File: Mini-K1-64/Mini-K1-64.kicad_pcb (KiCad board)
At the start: 2 copper layers, 55 x 44.6 mm, 47 parts, among them J2 Conn_01x16_Pin, J3 Conn_01x16_Pin, J4 Conn_01x16_Pin, J5 Conn_01x16_Pin, P1 USB_C_Plug_USB2.0, SW1 KEY, U1 CH343G, U2 FS32K144HAT0MLHT, U3 AMS1117-3.3, Y1 8M

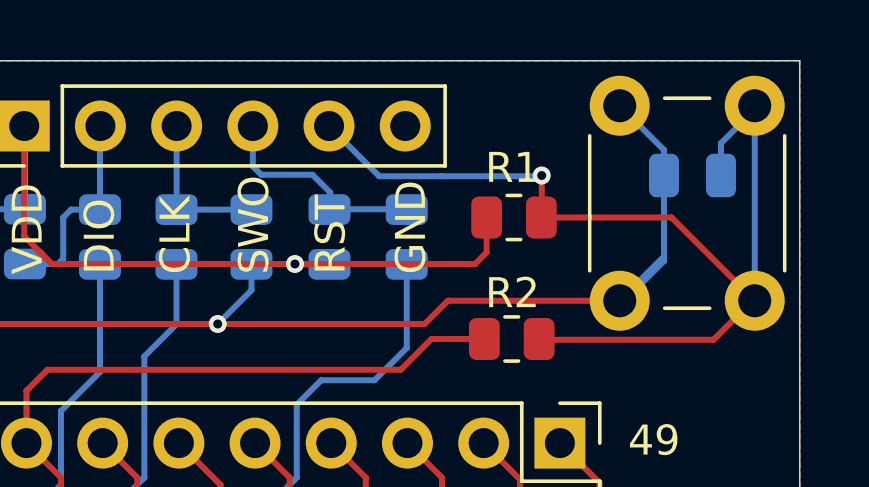
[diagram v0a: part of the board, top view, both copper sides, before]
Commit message: Fix via position
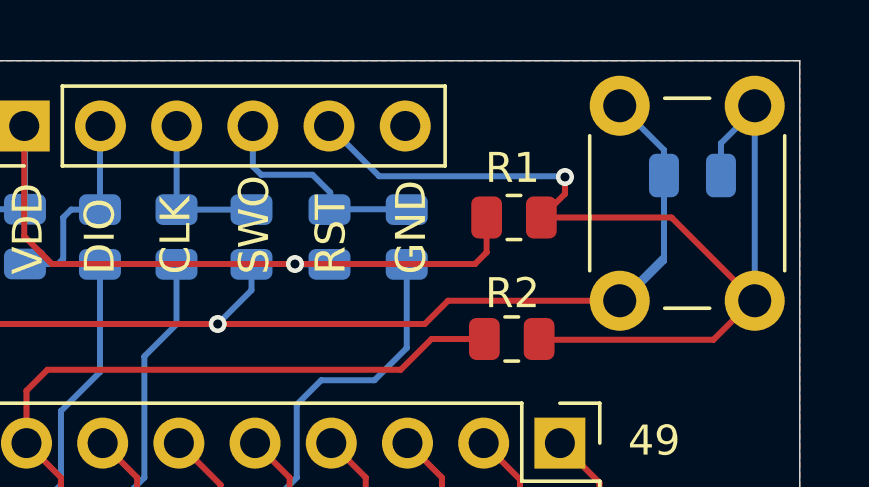
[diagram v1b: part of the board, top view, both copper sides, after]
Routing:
- net /MCU/RESET: track 34.5 -> 35.5 mm
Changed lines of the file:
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@@
 	)
 	(segment
-		(start 160.56 84.2625)
+		(start 161.335 83.4875)
 		(end 160.5475 84.275)
 		(width 0.2)
@@
 	)
 	(segment
-		(start 164.885 84.275)
-		(end 167.66 87.05)
+		(start 161.335 82.925)
+		(end 161.335 83.4875)
 		(width 0.2)
 		(layer "F.Cu")
@@
 	)
 	(segment
-		(start 160.56 82.875)
-		(end 160.56 84.2625)
+		(start 164.885 84.275)
+		(end 167.66 87.05)
 		(width 0.2)
 		(layer "F.Cu")
@@
 	)
 	(via
-		(at 160.56 82.875)
+		(at 161.335 82.925)
 		(size 0.6)
 		(drill 0.3)
@@
 	)
 	(segment
-		(start 157.185 82.9)
-		(end 160.535 82.9)
-		(width 0.2)
-		(layer "B.Cu")
-		(net 7)
-	)
-	(segment
-		(start 155.145 82.9)
-		(end 157.185 82.9)
+		(start 161.31 82.9)
+		(end 155.145 82.9)
 		(width 0.2)
 		(layer "B.Cu")
@@
 	)
 	(segment
+		(start 155.145 82.9)
+		(end 153.47 81.225)
+		(width 0.2)
+		(layer "B.Cu")
+		(net 7)
+	)
+	(segment
 		(start 166.535 81.8)
 		(end 166.535 82.875)
@@
 	)
 	(segment
-		(start 153.47 81.225)
-		(end 155.145 82.9)
+		(start 161.335 82.925)
+		(end 161.31 82.9)
 		(width 0.2)
 		(layer "B.Cu")
-		(net 7)
-	)
-	(segment
-		(start 160.535 82.9)
-		(end 160.56 82.875)
-		(width 0.2)
-		(layer "B.Cu")

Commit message: Format PCB
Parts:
- C1: renamed from C8; moved to F.Cu
- C11: renamed from C1; moved to B.Cu
- C12: renamed from C2; moved to B.Cu
- R11: renamed from R1; moved to B.Cu
- R2: renamed from R11; moved to F.Cu
- R3: renamed from R12; moved to F.Cu
- moved R15 13.5 mm to (123.6, 120.6), turned to -90 degrees
- moved R14 10.8 mm to (126.2, 120.6), turned to -90 degrees
- moved R11 10.3 mm to (167.7, 90.7), turned to 90 degrees
- moved R1 7.34 mm to (166.7, 89.8)
- moved C12 6.63 mm to (132.3, 117.4)
- moved C11 6.34 mm to (134.4, 117.4)
- moved Y1 5.20 mm to (135.7, 120.3)
- moved C1 4.62 mm to (125.8, 92.2), turned to 0 degrees
- moved C4 3.29 mm to (160.3, 105.6), turned to 90 degrees
- moved R3 2.79 mm to (132.3, 114.7), turned to -90 degrees
- moved R7 2.57 mm to (153.5, 84.9)
- moved R9 2.57 mm to (156.1, 84.9)
- moved R2 1.81 mm to (134.4, 114.7), turned to -90 degrees
- moved U1 1.46 mm to (124.2, 98.8)
- moved R12 1.46 mm to (124.5, 95.5), turned to 180 degrees
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- renumbered C12 to C10, C3 to C2, C4 to C3, C5 to C4, C6 to C5, C7 to C6, C9 to C7, C10 to C8, C11 to C9, H2 to H1, H1 to H2, JP3 to JP2, JP2 to JP3, R2 to R1, R9 to R10, R10 to R12, R7 to R4, R6 to R5, R5 to R6, R3 to R7, R4 to R9
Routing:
- net /MCU/PTC2: track 22.9 -> 41.2 mm
- net VDD: track 111.3 -> 129.6 mm, vias 2 -> 1
- net /USBUART/OGND: track 108.9 -> 93.5 mm
- net /MCU/PTC3: track 17.9 -> 33.2 mm
- net /MCU/UART_RX: track 39.5 -> 26.8 mm
- net GNDD: track 150.3 -> 162.1 mm
- net /MCU/UART_TX: track 36.3 -> 25.7 mm
- net /MCU/PTA5: track 29.4 -> 35.8 mm
- net /MCU/RESET: track 35.5 -> 30.3 mm, vias 1 -> 0
- net Net-(C12-Pad1): track 11.3 -> 7.97 mm
- net Net-(C11-Pad1): track 10.1 -> 7.80 mm
- net /MCU/PTA10: track 18.7 -> 16.6 mm
- net /MCU/PTC15: track 11.1 -> 12.5 mm
- net /JTAG/SWDIO: track 6.85 -> 8.20 mm
- net /USBUART/UD+: track 16.8 -> 15.6 mm
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
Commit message: Add Symbol
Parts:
- removed G***: LOGO, WTMEC:WTLogo
- added LOGO1: ~, WTMEC:WTLogo, F.Cu at (135.3, 86.4)

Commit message: Step Update
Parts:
- removed P1: USB_C_Plug_USB2.0, Connector_USB:USB_C_Receptacle_GCT_USB4105-xx-A_16P_TopMnt_Horizontal
- added J6: USB_C_Receptacle_USB2.0_14P, Connector_USB:USB_C_Receptacle_GCT_USB4105-xx-A_16P_TopMnt_Horizontal, F.Cu at (122.9, 82.8)
- added R16: 5.1K, Resistor_SMD:R_0805_2012Metric, B.Cu at (120.0, 82.6)
- R15: value 0 -> 10K
- U1: value CH343G -> CH340N; footprint Package_SO:SOIC-16_3.9x9.9mm_P1.27mm -> Package_SO:SOP-8_3.9x4.9mm_P1.27mm
- moved C7 6.71 mm to (118.9, 102.2)
- moved D1 5.74 mm to (122.2, 86.2), turned to 90 degrees
- moved R12 5.48 mm to (124.7, 90.0)
- moved JP1 5.41 mm to (126.3, 100.4)
- moved U1 5.40 mm to (121.7, 94.0)
- moved R10 5.28 mm to (125.1, 83.6)
- moved C10 4.65 mm to (121.2, 90.1), turned to 180 degrees
- moved C1 2.09 mm to (126.7, 94.1), turned to 90 degrees
- moved U3 1.44 mm to (119.9, 95.5)
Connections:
- U1 pad 1: /USBUART/OGND -> /USBUART/UD+
- U1 pad 2: /MCU/UART_RX -> /USBUART/UD-
- U1 pad 3: /MCU/UART_TX -> /USBUART/OGND
- U1 pad 4: Net-(U1-V3) -> unconnected-(U1-~{RTS}-Pad4)
- U1 pad 5: /USBUART/UD+ -> VBUS
- U1 pad 6: /USBUART/UD- -> /MCU/UART_RX
- U1 pad 7: VBUS -> /MCU/UART_TX
- U1 pad 8: unconnected-(U1-~{ACT}-Pad8) -> Net-(U1-V3)
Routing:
- net VBUS: track 42.6 -> 27.6 mm
- net /USBUART/OGND: track 93.5 -> 85.1 mm
- net /USBUART/UD+: track 15.6 -> 8.33 mm
- net Net-(JP1-B): track 24.7 -> 18.4 mm
- net VDDA: track 36.1 -> 29.9 mm
- net /USBUART/UD-: track 10.8 -> 5.15 mm
- net Net-(J6-CC2): track 0.00 -> 3.77 mm, vias 0 -> 1
- net /MCU/UART_RX: track 26.8 -> 24.1 mm, vias 3 -> 1
- net /MCU/UART_TX: track 25.7 -> 24.7 mm, vias 3 -> 1
- net GNDA: track 36.1 -> 35.9 mm, vias 5 -> 2

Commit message: Rev0
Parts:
- moved U3 8.59 mm to (119.8, 104.1)
- moved C7 7.41 mm to (118.9, 109.6)
- moved D1 5.49 mm to (119.0, 90.7), turned to 180 degrees
- moved JP1 5.40 mm to (126.3, 105.8)
- moved C10 3.27 mm to (119.8, 93.0)
- moved R13 3.20 mm to (123.5, 93.0)
- moved R10 1.74 mm to (120.3, 84.3), turned to 180 degrees
- moved C2 0.64 mm to (165.6, 83.5)
- moved SW1 0.64 mm to (163.2, 87.7)
- moved J1 0.62 mm to (122.9, 83.4)
- moved C1 0.62 mm to (126.7, 94.7)
- moved R11 0.62 mm to (125.1, 84.2)
- moved U1 0.62 mm to (121.6, 94.6)
- moved R1 0.45 mm to (166.7, 90.3)
- moved J2 0.26 mm to (143.3, 81.5)
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- renumbered J6 to J1, J1 to J2, J2 to J3, J3 to J4, J4 to J5, J5 to J6, R16 to R10, R10 to R11, R11 to R12, R12 to R13, R13 to R14, R14 to R15, R15 to R16
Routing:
- net VBUS: track 27.6 -> 34.9 mm
- net VDDA: track 29.9 -> 25.9 mm
- net /USBUART/OGND: track 85.1 -> 88.9 mm
- net /USBUART/UD-: track 5.15 -> 8.38 mm, vias 0 -> 2
- net Net-(JP1-B): track 18.4 -> 15.6 mm
- net VDD: track 129.6 -> 127.6 mm
- net Net-(J1-CC2): track 3.77 -> 2.76 mm
- net /USBUART/UD+: track 8.33 -> 9.23 mm, vias 1 -> 3
- net GNDD: track 162.1 -> 161.4 mm
- net /MCU/RESET: track 30.3 -> 29.6 mm
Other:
- board size 55 x 44.6 mm -> 55 x 44 mm
- board text added: "K1-64_V0 2024.05.12"
- board text removed: "K1-64_V0 2024.05.06"

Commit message: Format PCB
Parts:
- moved R4 0.28 mm to (145.8, 85.5)
- moved R5 0.28 mm to (148.4, 85.5)
- moved R6 0.28 mm to (150.9, 85.5)
- moved R7 0.28 mm to (153.5, 85.5)
- moved R8 0.28 mm to (143.3, 85.5)
- moved R9 0.28 mm to (156.1, 85.5)
- moved J2 0.28 mm to (143.3, 81.8)
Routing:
- net GNDD: track 161.4 -> 174.7 mm
- net /USBUART/OGND: track 88.9 -> 95.4 mm
- net /MCU/PTA10: track 16.6 -> 17.7 mm
- net /MCU/UART_RX: track 24.1 -> 23.5 mm
- net VDD: track 127.6 -> 127.0 mm
- net GNDA: vias 2 -> 3

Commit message: Update Gerber
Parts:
- moved R1 2.57 mm to (167.0, 92.8)
- moved R12 2.22 mm to (167.0, 92.8), turned to 0 degrees
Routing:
- net /MCU/RESET: track 29.5 -> 35.2 mm
- net /MCU/PTA5: track 36.0 -> 38.5 mm
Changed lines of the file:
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@@
 	(footprint "Resistor_SMD:R_0805_2012Metric"
 		(layer "F.Cu")
-		(at 166.738 90.274 180)
+		(at 166.96 92.835 180)
 		(descr "Resistor SMD 0805 (2012 Metric), square (rectangular) end terminal, IPC_7351 nominal, (Body size source: IPC-SM-782 page 72, https://www.pcb-3d.com/wordpress/wp-content/uploads/ipc-sm-782a_amendment_1_and_2.pdf), generated with kicad-footprint-generator")
 		(tags "resistor")
 		(property "Reference" "R1"
-			(at -0.9625 -1.8 180)
+			(at 0 1.58 180)
 			(layer "F.SilkS")
 			(effects
@@
 	(footprint "Resistor_SMD:R_0805_2012Metric"
 		(layer "B.Cu")
-		(at 167.66 90.725 90)
+		(at 166.96 92.835)
 		(descr "Resistor SMD 0805 (2012 Metric), square (rectangular) end terminal, IPC_7351 nominal, (Body size source: IPC-SM-782 page 72, https://www.pcb-3d.com/wordpress/wp-content/uploads/ipc-sm-782a_amendment_1_and_2.pdf), generated with kicad-footprint-generator")
 		(tags "resistor")
 		(property "Reference" "R12"
-			(at -0.0062 -2.5222 0)
+			(at -0.0062 -2.5222 90)
 			(layer "B.SilkS")
 			(effects
@@
 		)
 		(property "Value" "10K"
-			(at 0 -1.65 -90)
+			(at 0 -1.65 360)
 			(layer "B.Fab")
 			(hide yes)
@@
 		)
 		(property "Footprint" "Resistor_SMD:R_0805_2012Metric"
-			(at 0 0 -90)
+			(at 0 0 180)
 			(unlocked yes)
 			(layer "B.Fab")
@@
 		)
 		(property "Datasheet" ""
-			(at 0 0 -90)
+			(at 0 0 180)
 			(unlocked yes)
 			(layer "B.Fab")
@@
 		)
 		(property "Description" "Resistor"
-			(at 0 0 -90)
+			(at 0 0 180)
 			(unlocked yes)
 			(layer "B.Fab")
@@
 		)
 		(fp_line
-			(start 1.68 -0.95)
-			(end 1.68 0.95)
+			(start -1.68 -0.95)
+			(end 1.68 -0.95)
 			(stroke
 				(width 0.05)
@@
 		)
 		(fp_line
-			(start -1.68 -0.95)
-			(end 1.68 -0.95)
+			(start -1.68 0.95)
+			(end -1.68 -0.95)
 			(stroke
 				(width 0.05)
@@
 		)
 		(fp_line
-			(start 1.68 0.95)
-			(end -1.68 0.95)
+			(start 1.68 -0.95)
+			(end 1.68 0.95)
 			(stroke
 				(width 0.05)
@@
 		)
 		(fp_line
-			(start -1.68 0.95)
-			(end -1.68 -0.95)
+			(start 1.68 0.95)
+			(end -1.68 0.95)
 			(stroke
 				(width 0.05)
@@
 		)
 		(fp_line
-			(start 1 -0.625)
-			(end 1 0.625)
+			(start -1 -0.625)
+			(end 1 -0.625)
 			(stroke
 				(width 0.1)
@@
 		)
 		(fp_line
-			(start -1 -0.625)
-			(end 1 -0.625)
+			(start -1 0.625)
+			(end -1 -0.625)
 			(stroke
 				(width 0.1)
@@
 		)
 		(fp_line
-			(start 1 0.625)
-			(end -1 0.625)
+			(start 1 -0.625)
+			(end 1 0.625)
 			(stroke
 				(width 0.1)
@@
 		)
 		(fp_line
-			(start -1 0.625)
-			(end -1 -0.625)
+			(start 1 0.625)
+			(end -1 0.625)
 			(stroke
 				(width 0.1)
@@
 		)
 		(fp_text user "${REFERENCE}"
-			(at 0 0 -90)
+			(at 0 0 360)
 			(layer "B.Fab")
 			(effects
@@
 		)
 		(pad "1" smd roundrect
-			(at -0.9125 0 90)
+			(at -0.9125 0)
 			(size 1.025 1.4)
 			(layers "B.Cu" "B.Paste" "B.Mask")
@@
 		)
 		(pad "2" smd roundrect
-			(at 0.9125 0 90)
+			(at 0.9125 0)
 			(size 1.025 1.4)
 			(layers "B.Cu" "B.Paste" "B.Mask")
@@
 	)
 	(gr_text "49"
-		(at 163.435 92.3 0)
+		(at 163.15 92.435 0)
 		(layer "F.SilkS")
 		(effects
@@
 	)
 	(gr_text "50"
-		(at 163.435 94.825 0)
+		(at 163.16 95.105 0)
 		(layer "F.SilkS")
 		(effects
@@
 	)
 	(segment
-		(start 157.0784 89.225)
-		(end 164.085 89.225)
-		(width 0.3)
-		(layer "B.Cu")
-		(net 1)
-	)
-	(segment
 		(start 156.0512 88.1978)
 		(end 157.0784 89.225)
@@
 	)
 	(segment
-		(start 166.4975 91.6375)
-		(end 167.66 91.6375)
-		(width 0.3)
-		(layer "B.Cu")
-		(net 1)
-	)
-	(segment
 		(start 132.4975 105.5)
 		(end 131.785 106.2125)
@@
 	)
 	(segment
-		(start 168.505 93.65)
-		(end 167.66 92.805)
-		(width 0.3)
-		(layer "B.Cu")
-		(net 1)
-	)
-	(segment
 		(start 140.36 104.275)
 		(end 138.525 104.275)
@@
 	)
 	(segment
+		(start 168.505 96.32)
+		(end 168.505 104.355)
+		(width 0.3)
+		(layer "B.Cu")
+		(net 1)
+	)
+	(segment
 		(start 143.3012 81.7628)
 		(end 143.3012 84.5253)
@@
 	)
 	(segment
-		(start 168.505 104.355)
-		(end 168.505 93.65)
-		(width 0.3)
-		(layer "B.Cu")
-		(net 1)
-	)
-	(segment
 		(start 143.3262 84.5503)
 		(end 143.3262 81.7878)
@@
 	)
 	(segment
-		(start 164.085 89.225)
-		(end 166.4975 91.6375)
+		(start 157.0784 89.225)
+		(end 165.32 89.225)
 		(width 0.3)
 		(layer "B.Cu")
@@
 	)
 	(segment
-		(start 134.26 105.5)
-		(end 132.4975 105.5)
-		(width 0.4)
+		(start 156.0512 86.3753)
+		(end 156.0512 88.1978)
+		(width 0.3)
 		(layer "B.Cu")
 		(net 1)
 	)
 	(segment
-		(start 167.66 92.805)
-		(end 167.66 91.6375)
+		(start 166.0475 93.8625)
+		(end 168.505 96.32)
 		(width 0.3)
 		(layer "B.Cu")
@@
 	)
 	(segment
+		(start 134.26 105.5)
+		(end 132.4975 105.5)
+		(width 0.4)
+		(layer "B.Cu")
+		(net 1)
+	)
+	(segment
 		(start 143.3012 84.5253)
 		(end 143.3262 84.5503)
@@
 	)
 	(segment
-		(start 156.0512 86.3753)
-		(end 156.0512 88.1978)
-		(width 0.3)
-		(layer "B.Cu")
-		(net 1)
-	)
-	(segment
 		(start 132.81 105.5)
 		(end 134.26 105.5)
@@
 	)
 	(segment
+		(start 165.32 89.225)
+		(end 166.0475 89.9525)
+		(width 0.3)
+		(layer "B.Cu")
+		(net 1)
+	)
+	(segment
 		(start 140.4975 95.5375)
 		(end 141.01 95.025)
@@
 	)
 	(segment
+		(start 166.0475 92.835)
+		(end 166.0475 93.8625)
+		(width 0.3)
+		(layer "B.Cu")
+		(net 1)
+	)
+	(segment
+		(start 166.0475 89.9525)
+		(end 166.0475 92.835)
+		(width 0.3)
+		(layer "B.Cu")
+		(net 1)
+	)
+	(segment
 		(start 141.51 105.425)
 		(end 142.91 105.425)
@@
 	)
 	(segment
+		(start 167.8725 90.496)
+		(end 167.65 90.2735)
+		(width 0.2)
+		(layer "F.Cu")
+		(net 7)
+	)
+	(segment
 		(start 167.65 87.685)
 		(end 167.65 90.2735)
@@
 	)
 	(segment
-		(start 167.65 90.2735)
-		(end 167.6505 90.274)
+		(start 167.8725 92.835)
+		(end 167.8725 90.496)
 		(width 0.2)
 		(layer "F.Cu")
@@
 	)
 	(segment
-		(start 167.66 89.8125)
-		(end 167.66 87.695)
-		(width 0.4)
+		(start 167.65 90.385)
+		(end 167.65 87.685)
+		(width 0.2)
 		(layer "B.Cu")
 		(net 7)
@@
 	)
 	(segment
-		(start 167.66 87.695)
-		(end 167.65 87.685)
-		(width 0.4)
+		(start 167.8725 92.835)
+		(end 167.8725 90.6075)
+		(width 0.2)
 		(layer "B.Cu")
 		(net 7)
@@
 	)
 	(segment
+		(start 167.8725 90.6075)
+		(end 167.65 90.385)
+		(width 0.2)
+		(layer "B.Cu")
+		(net 7)
+	)
+	(segment
 		(start 166.525 84.51)
 		(end 166.225 84.81)
@@
 	)
 	(segment
-		(start 165.8255 90.274)
-		(end 164.2152 90.274)
+		(start 163.7662 89.825)
+		(end 143.86 89.825)
 		(width 0.2)
 		(layer "F.Cu")
@@
 	)
 	(segment
-		(start 163.7662 89.825)
-		(end 143.86 89.825)
+		(start 166.0475 92.835)
+		(end 166.0475 90.7815)
 		(width 0.2)
 		(layer "F.Cu")
@@
 	)
 	(segment
+		(start 165.54 90.274)
+		(end 164.2152 90.274)
+		(width 0.2)
+		(layer "F.Cu")
+		(net 56)
+	)
+	(segment
 		(start 143.86 89.825)
 		(end 143.385 90.3)
@@
 	)
 	(segment
+		(start 166.0475 90.7815)
+		(end 165.54 90.274)
+		(width 0.2)
+		(layer "F.Cu")
+		(net 56)
+	)
+	(segment
 		(start 157.36 93.07)
 		(end 156.085 91.795)
@@
 		(polygon
 			(pts
-				(xy 114.16 123.675) (xy 119.235 123.675) (xy 119.235 115.8) (xy 119.235 115.8) (xy 119.16 103.675)
-				(xy 129.96 103.675) (xy 129.96 79.675) (xy 114.16 79.675)
+				(xy 114.16 123.675) (xy 119.235 123.675) (xy 119.235 115.8) (xy 119.16 103.675) (xy 129.96 103.675)
+				(xy 129.96 79.675) (xy 114.16 79.675)
 			)
 		)
@@
 			(pts
 				(xy 129.96 103.675) (xy 129.96 117.555) (xy 127.19 117.555) (xy 127.18 123.685) (xy 119.235 123.675)
-				(xy 119.235 115.8) (xy 119.235 115.8) (xy 119.16 103.675)
+				(xy 119.235 115.8) (xy 119.16 103.675)
 			)
 		)

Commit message: Format PCB
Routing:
- net GNDD: vias 8 -> 13
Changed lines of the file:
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@@
 		(tags "resistor")
 		(property "Reference" "R12"
-			(at -0.0062 -2.5222 90)
+			(at -0.02 -1.62 180)
 			(layer "B.SilkS")
 			(effects
@@
 		)
 		(property "Value" "10K"
-			(at 0 -1.65 360)
+			(at 0 -1.65 0)
 			(layer "B.Fab")
 			(hide yes)
@@
 		)
 		(fp_text user "${REFERENCE}"
-			(at 0 0 360)
+			(at 0 0 0)
 			(layer "B.Fab")
 			(effects
@@
 	)
 	(segment
-		(start 133.6475 95.5375)
-		(end 140.4975 95.5375)
-		(width 0.2)
-		(layer "B.Cu")
-		(net 1)
-	)
-	(segment
 		(start 167.305 105.555)
 		(end 168.505 104.355)
@@
 	)
 	(segment
-		(start 132.81 96.375)
-		(end 133.6475 95.5375)
+		(start 132.81 86.375)
+		(end 134.6347 84.5503)
 		(width 0.2)
 		(layer "B.Cu")
@@
 	)
 	(segment
-		(start 142.3373 84.5503)
-		(end 143.3262 84.5503)
-		(width 0.2)
-		(layer "B.Cu")
-		(net 1)
-	)
-	(segment
 		(start 156.41 106.575)
 		(end 162.085 106.575)
@@
 	)
 	(segment
+		(start 134.6347 84.5503)
+		(end 143.3262 84.5503)
+		(width 0.2)
+		(layer "B.Cu")
+		(net 1)
+	)
+	(segment
 		(start 152.96 105.425)
 		(end 154.11 106.575)
@@
 	)
 	(segment
-		(start 141.01 95.025)
-		(end 141.01 85.8776)
+		(start 132.81 105.5)
+		(end 132.81 86.375)
 		(width 0.2)
 		(layer "B.Cu")
@@
 	)
 	(segment
-		(start 141.01 85.8776)
-		(end 142.3373 84.5503)
-		(width 0.2)
-		(layer "B.Cu")
-		(net 1)
-	)
-	(segment
 		(start 143.3262 81.7878)
 		(end 143.3012 81.7628)
@@
 	(segment
 		(start 132.81 105.5)
-		(end 132.81 96.375)
-		(width 0.2)
-		(layer "B.Cu")
-		(net 1)
-	)
-	(segment
-		(start 132.81 105.5)
 		(end 134.26 105.5)
 		(width 0.4)
@@
 	)
 	(segment
-		(start 140.4975 95.5375)
-		(end 141.01 95.025)
-		(width 0.2)
-		(layer "B.Cu")
-		(net 1)
-	)
-	(segment
 		(start 166.0475 92.835)
 		(end 166.0475 93.8625)
@@
 	)
 	(via
+		(at 141.16 82.675)
+		(size 0.6)
+		(drill 0.3)
+		(layers "F.Cu" "B.Cu")
+		(free yes)
+		(net 2)
+	)
+	(via
 		(at 150.8762 88.8856)
 		(size 0.6)
@@
 	)
 	(via
+		(at 131.16 96.675)
+		(size 0.6)
+		(drill 0.3)
+		(layers "F.Cu" "B.Cu")
+		(free yes)
+		(net 2)
+	)
+	(via
 		(at 132.785 109.375)
 		(size 0.6)
@@
 	)
 	(via
+		(at 136.16 82.675)
+		(size 0.6)
+		(drill 0.3)
+		(layers "F.Cu" "B.Cu")
+		(free yes)
+		(net 2)
+	)
+	(via
+		(at 131.16 89.675)
+		(size 0.6)
+		(drill 0.3)
+		(layers "F.Cu" "B.Cu")
+		(free yes)
+		(net 2)
+	)
+	(via
 		(at 149.735 103.525)
 		(size 0.6)
@@
 		(net 2)
 	)
+	(via
+		(at 131.16 82.675)
+		(size 0.6)
+		(drill 0.3)
+		(layers "F.Cu" "B.Cu")
+		(free yes)
+		(net 2)
+	)
 	(segment
 		(start 155.61 103.525)
@@
 	)
 	(segment
-		(start 164.2152 90.274)
-		(end 163.7662 89.825)
+		(start 143.86 89.825)
+		(end 165.67 89.825)
 		(width 0.2)
 		(layer "F.Cu")
@@
 	)
 	(segment
-		(start 163.7662 89.825)
+		(start 143.385 90.3)
 		(end 143.86 89.825)
 		(width 0.2)
@@
 	)
 	(segment
-		(start 166.0475 92.835)
-		(end 166.0475 90.7815)
-		(width 0.2)
-		(layer "F.Cu")
-		(net 56)
-	)
-	(segment
-		(start 144.66 95.384314)
-		(end 149.025 99.749314)
-		(width 0.2)
-		(layer "F.Cu")
-		(net 56)
-	)
-	(segment
 		(start 143.385 91.795)
 		(end 143.385 90.3)
@@
 	)
 	(segment
-		(start 165.54 90.274)
-		(end 164.2152 90.274)
+		(start 166.0475 92.835)
+		(end 166.0475 90.2025)
 		(width 0.2)
 		(layer "F.Cu")
@@
 	)
 	(segment
-		(start 143.86 89.825)
-		(end 143.385 90.3)
+		(start 144.66 95.384314)
+		(end 149.025 99.749314)
 		(width 0.2)
 		(layer "F.Cu")
@@
 	)
 	(segment
-		(start 166.0475 90.7815)
-		(end 165.54 90.274)
+		(start 166.0475 90.2025)
+		(end 165.67 89.825)
 		(width 0.2)
 		(layer "F.Cu")
@@
 			(thermal_gap 0.5)
 			(thermal_bridge_width 0.5)
+			(smoothing fillet)
+			(radius 1)
 		)
 		(polygon
@@
 			(thermal_gap 0.5)
 			(thermal_bridge_width 0.5)
+			(smoothing fillet)
+			(radius 1)
 		)
 		(polygon
@@
 			(thermal_gap 0.5)
 			(thermal_bridge_width 0.5)
+			(smoothing fillet)
+			(radius 1)
 		)
 		(polygon
